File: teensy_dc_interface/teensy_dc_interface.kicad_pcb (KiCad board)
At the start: 2 copper layers, 183 parts, among them J1 3.5mm_Mono_Switched_SymSmall_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, J10 Conn_01x03, J11 Conn_01x03, J12 3.5mm_Mono_Switched_SymSmall_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, J13 3.5mm_Mono_Switched_SymSmall_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, J2 3.5mm_Mono_Switched_SymSmall_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, J3 3.5mm_Mono_Switched_SymSmall_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, J4 3.5mm_Mono_Switched_SymSmall_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, J5 3.5mm_Mono_Switched_SymSmall_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, J6 3.5mm_Mono_Switched_SymSmall_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, J7 3.5mm_Mono_Switched_SymSmall_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, J8 3.5mm_Mono_Switched_SymSmall_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, J9 Conn_01x03, U1 AK4458VN, U2 Teensy4.0, U3 AP65211A, U4 AP62200TWU-7, U5 NE5532, U6 NE5532, U7 NE5532, U8 NE5532, U9 AP65211A

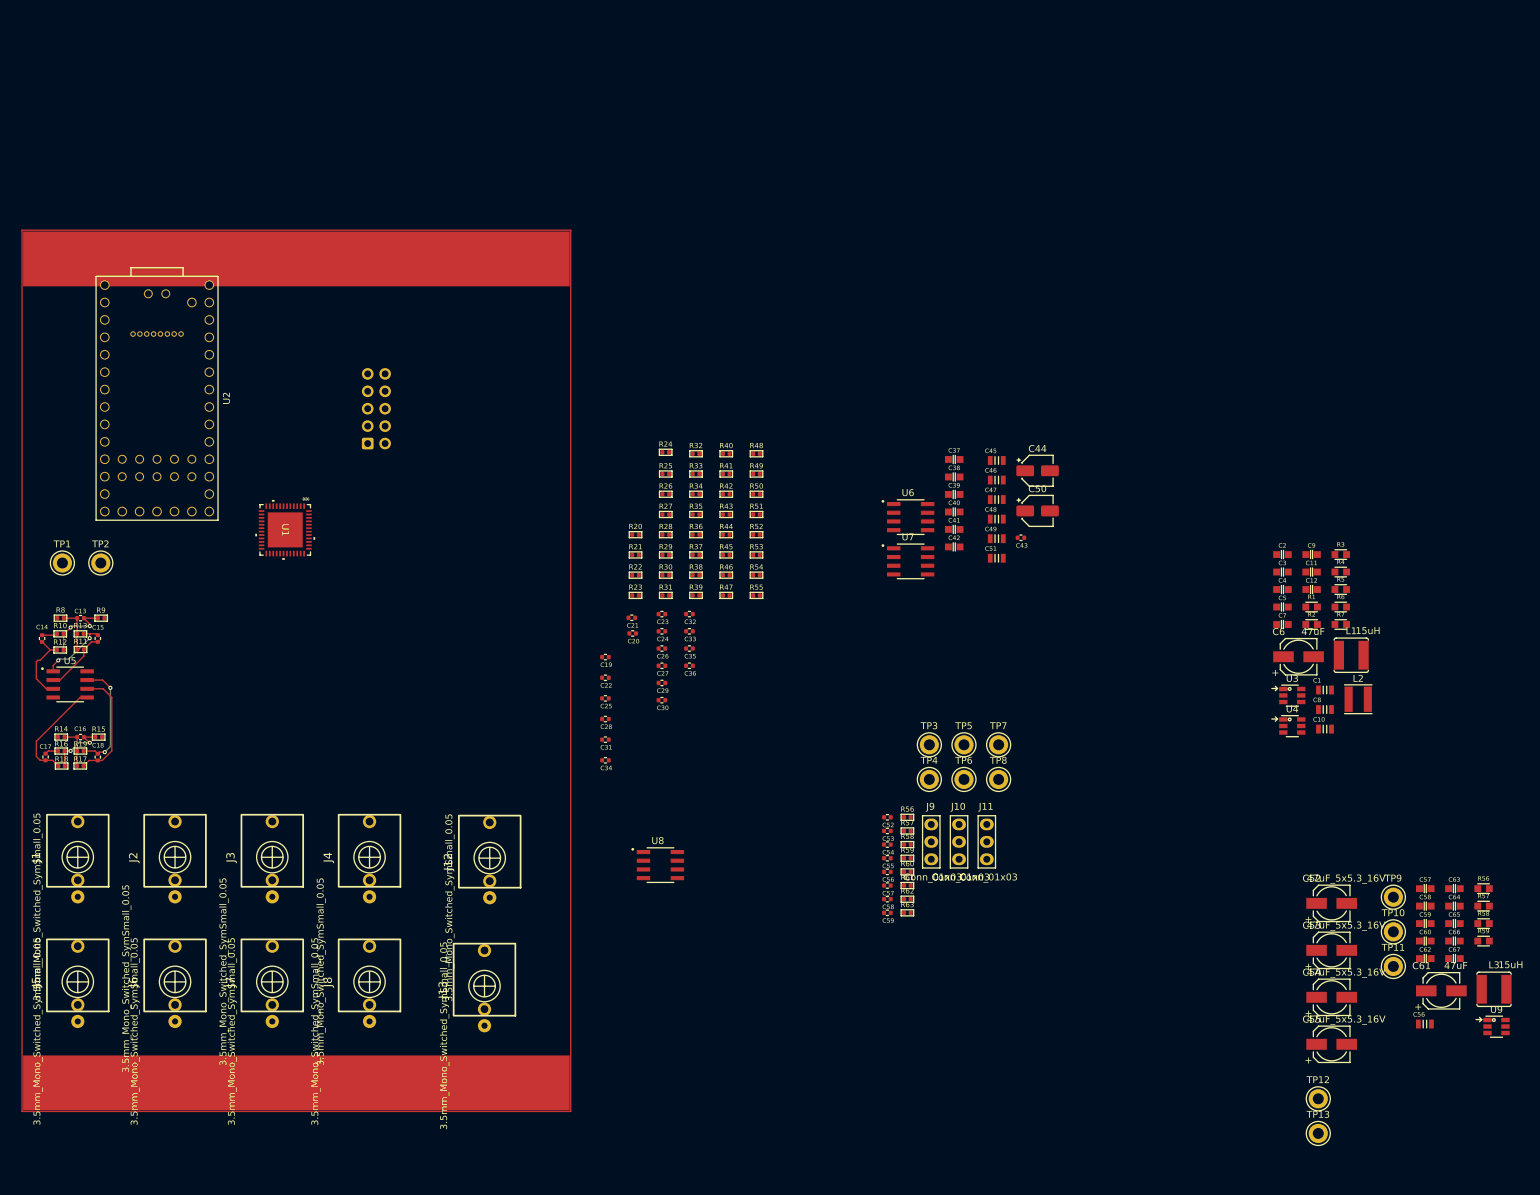
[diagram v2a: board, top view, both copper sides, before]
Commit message: out pairs as pages
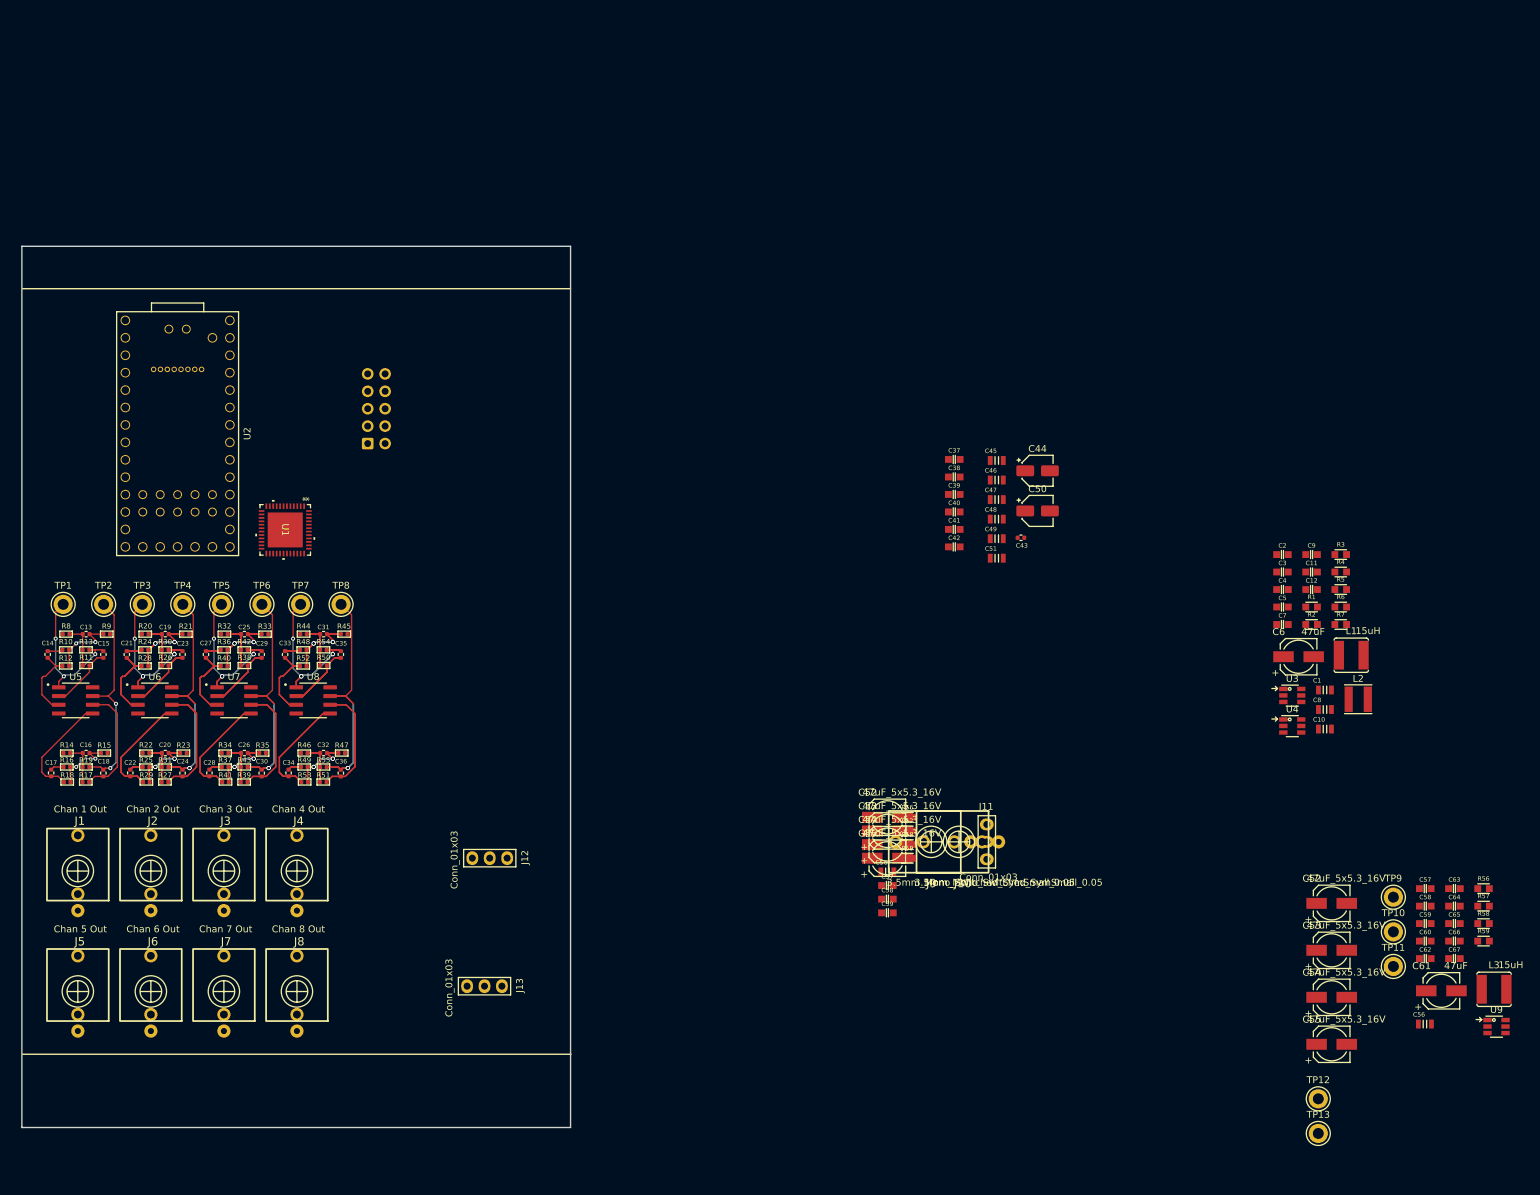
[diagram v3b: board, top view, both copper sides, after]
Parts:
- removed ?: , 
- removed R60, R61, R62, R63: 10R_0402, 4ms_Resistor:R_0402
- removed REF**: Rail_Connection_16HP, 4ms_Faceplate:Rail_Connection_16HP
- C20, C26, C32: value 120p -> 1.0n
- C22, C28, C34: value 1.0n -> 120p
- C52, C53, C54, C55: value 220pF_0402_50V -> 47uF_5x5.3_16V; footprint 4ms_Capacitor:C_0402 -> 4ms_Capacitor:CP_Elec_5x5.3
- C56: value 220pF_0402_50V -> 22uF; footprint 4ms_Capacitor:C_0402 -> 4ms_Capacitor:C_0805
- C57: value 220pF_0402_50V -> 0.1uF; footprint 4ms_Capacitor:C_0402 -> 4ms_Capacitor:C_0603
- C58: value 220pF_0402_50V -> 47pF; footprint 4ms_Capacitor:C_0402 -> 4ms_Capacitor:C_0603
- C59: value 220pF_0402_50V -> 22uF; footprint 4ms_Capacitor:C_0402 -> 4ms_Capacitor:C_0603
- J1: value 3.5mm_Mono_Switched_SymSmall_0.05 -> Chan 1 Out
- J10, J9: value Conn_01x03 -> 3.5mm_Mono_Switched_SymSmall_0.05; footprint 4ms_Connector:Pins_1x03_2.54mm_TH -> 4ms_Jack:EighthInch_PJ398SM
- J12, J13: value 3.5mm_Mono_Switched_SymSmall_0.05 -> Conn_01x03; footprint 4ms_Jack:EighthInch_PJ398SM -> 4ms_Connector:Pins_1x03_2.54mm_TH
- J2: value 3.5mm_Mono_Switched_SymSmall_0.05 -> Chan 2 Out
- J3: value 3.5mm_Mono_Switched_SymSmall_0.05 -> Chan 3 Out
- J4: value 3.5mm_Mono_Switched_SymSmall_0.05 -> Chan 4 Out
- J5: value 3.5mm_Mono_Switched_SymSmall_0.05 -> Chan 5 Out
- J6: value 3.5mm_Mono_Switched_SymSmall_0.05 -> Chan 6 Out
- J7: value 3.5mm_Mono_Switched_SymSmall_0.05 -> Chan 7 Out
- J8: value 3.5mm_Mono_Switched_SymSmall_0.05 -> Chan 8 Out
- R22, R34, R46: value 16.9k -> 3.9k
- R23, R35, R47: value 150 -> 3.9k
- R24, R30, R36, R42, R48, R54: value 150 -> 16.9k
- R26, R27, R38, R39, R50, R51: value 3.9k -> 150
- R28, R40, R52: value 16.9k -> 150
- R56: value 10R_0402 -> 100k; footprint 4ms_Resistor:R_0402 -> 4ms_Resistor:R_0603
- R57: value 10R_0402 -> 75k; footprint 4ms_Resistor:R_0402 -> 4ms_Resistor:R_0603
- R58: value 10R_0402 -> 40.2k; footprint 4ms_Resistor:R_0402 -> 4ms_Resistor:R_0603
- R59: value 10R_0402 -> 7.68k; footprint 4ms_Resistor:R_0402 -> 4ms_Resistor:R_0603
- moved TP3 116.6 mm to (48.7, 73.2)
- moved U6 113.4 mm to (50.5, 87.2)
- moved TP4 111.8 mm to (54.6, 73.2)
- moved TP5 110.2 mm to (60.2, 73.2)
- moved TP6 105.5 mm to (66.1, 73.2)
- moved TP7 103.8 mm to (71.7, 73.2)
- moved U7 100.7 mm to (62.0, 87.2)
- moved TP8 99.2 mm to (77.6, 73.2)
- moved R25 87.0 mm to (49.2, 96.9)
- moved R41 85.7 mm to (60.8, 99.1), turned to 180 degrees
- moved R27 82.8 mm to (52.0, 99.1)
- moved R29 82.7 mm to (49.2, 99.1), turned to 180 degrees
- moved R24 81.2 mm to (49.0, 79.9)
- moved R40 79.5 mm to (60.6, 82.2), turned to 180 degrees
- moved R43 79.3 mm to (63.5, 96.9)
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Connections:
- net AOUTL1N renamed /DAC/AOUTL1N
- net AOUTL2N renamed /DAC/AOUTL2N
- net AOUTR1N renamed /DAC/AOUTR1N
- net OP1_NEG renamed /Outs/Out Pair 1/OP1_NEG
- net OP1_OUT renamed /Outs/Out Pair 1/OP1_OUT
- net OP1_POS renamed /Outs/Out Pair 1/OP1_POS
- net OP2_NEG renamed /Outs/Out Pair 1/OP2_NEG
- net OP2_OUT renamed /Outs/Out Pair 1/OP2_OUT
- net OP2_POS renamed /Outs/Out Pair 1/OP2_POS
- net OP4_OUT renamed /Outs/Out Pair 2/OP2_OUT
- net OP6_OUT renamed /Outs/Out Pair 3/OP2_OUT
- net OP8_OUT renamed /Outs/Out Pair 4/OP2_OUT
- C20 pad 1: OP3_POS -> Net-(C20-Pad1)
- C20 pad 2: AVSS -> Net-(C20-Pad2)
- C21 pad 1: OP3_NEG -> /Outs/Out Pair 2/OP1_POS
- C21 pad 2: OP3_OUT -> AVSS
- C22 pad 1: Net-(C22-Pad1) -> /Outs/Out Pair 2/OP2_POS
- C22 pad 2: Net-(C22-Pad2) -> AVSS
- C23 pad 1: OP4_POS -> /Outs/Out Pair 2/OP1_NEG
- C23 pad 2: AVSS -> /Outs/Out Pair 2/OP1_OUT
- C24 pad 1: OP4_NEG -> /Outs/Out Pair 2/OP2_NEG
- C26 pad 1: OP5_POS -> Net-(C26-Pad1)
- C26 pad 2: AVSS -> Net-(C26-Pad2)
- C27 pad 1: OP5_NEG -> /Outs/Out Pair 3/OP1_POS
- C27 pad 2: OP5_OUT -> AVSS
- C28 pad 1: Net-(C28-Pad1) -> /Outs/Out Pair 3/OP2_POS
- C28 pad 2: Net-(C28-Pad2) -> AVSS
- C29 pad 1: OP6_POS -> /Outs/Out Pair 3/OP1_NEG
- C29 pad 2: AVSS -> /Outs/Out Pair 3/OP1_OUT
- C30 pad 1: OP6_NEG -> /Outs/Out Pair 3/OP2_NEG
- C32 pad 1: OP7_POS -> Net-(C32-Pad1)
- C32 pad 2: AVSS -> Net-(C32-Pad2)
- C33 pad 1: OP7_NEG -> /Outs/Out Pair 4/OP1_POS
- C33 pad 2: OP7_OUT -> AVSS
- C34 pad 1: Net-(C34-Pad1) -> /Outs/Out Pair 4/OP2_POS
- C34 pad 2: Net-(C34-Pad2) -> AVSS
- C35 pad 1: OP8_POS -> /Outs/Out Pair 4/OP1_NEG
- C35 pad 2: AVSS -> /Outs/Out Pair 4/OP1_OUT
- C36 pad 1: OP8_NEG -> /Outs/Out Pair 4/OP2_NEG
- C52 pad 1: AOUTR4P -> AVDD
- C52 pad 2: Net-(C52-Pad2) -> AVSS
- C53 pad 1: AOUTL4P -> AVDD
- C53 pad 2: Net-(C53-Pad2) -> AVSS
- C54 pad 1: AOUTR3P -> AVDD
- C54 pad 2: Net-(C54-Pad2) -> AVSS
- C55 pad 1: AOUTL3P -> AVDD
- C55 pad 2: Net-(C55-Pad2) -> AVSS
- C56 pad 1: AOUTR2P -> +12V
- C56 pad 2: Net-(C56-Pad2) -> AVSS
- C57 pad 1: AOUTL2P -> /Power/SW
- C57 pad 2: Net-(C57-Pad2) -> /Power/BST
- C58 pad 1: AOUTR1P -> /Power/FB
- C58 pad 2: Net-(C58-Pad2) -> TEENSY_5V
- C59 pad 1: AOUTL1P -> TEENSY_5V
- C59 pad 2: Net-(C59-Pad2) -> AVSS
- J10 pad 1: DVSS -> ADC3
- J10 pad 2: SDTI3/DSDR2/TDMO1 -> AVSS
- J10 pad 3: 9_OUT1C -> AVSS
- J11 pad 2: SDTI4/DSDL3/TDMO2 -> SDTI2/DSDL2
- J11 pad 3: 6_OUT1D -> 32_OUT1B
- J12 pad 1: ADC2 -> DVSS
- J12 pad 2: AVSS -> SDTI3/DSDR2/TDMO1
- J12 pad 3: AVSS -> 9_OUT1C
- J13 pad 1: ADC3 -> DVSS
- J13 pad 2: AVSS -> SDTI4/DSDL3/TDMO2
- J13 pad 3: AVSS -> 6_OUT1D
- J3 pad 1: OP3_OUT -> /Outs/Out Pair 2/OP1_OUT
- J5 pad 1: OP5_OUT -> /Outs/Out Pair 3/OP1_OUT
- J7 pad 1: OP7_OUT -> /Outs/Out Pair 4/OP1_OUT
- J9 pad 1: DVSS -> ADC2
- J9 pad 2: SDTI2/DSDL2 -> AVSS
- J9 pad 3: 32_OUT1B -> AVSS
- R15 pad 1: AOUTR1P -> /DAC/AOUTR1P
- R21 pad 1: AOUTL2P -> /DAC/AOUTL2P
- R22 pad 1: AVSS -> /DAC/AOUTR2N
- R22 pad 2: Net-(C19-Pad2) -> Net-(C20-Pad1)
- R23 pad 1: Net-(C19-Pad1) -> /DAC/AOUTR2P
- R23 pad 2: OP3_NEG -> Net-(C20-Pad2)
- R24 pad 1: Net-(C19-Pad2) -> AVSS
- R24 pad 2: OP3_POS -> Net-(C19-Pad2)
- R25 pad 1: Net-(C19-Pad1) -> AVSS
- R25 pad 2: OP3_OUT -> Net-(C20-Pad2)
- R26 pad 1: AOUTR2N -> Net-(C19-Pad1)
- R26 pad 2: Net-(C22-Pad1) -> /Outs/Out Pair 2/OP1_NEG
- R27 pad 1: AOUTR2P -> Net-(C20-Pad1)
- R27 pad 2: Net-(C22-Pad2) -> /Outs/Out Pair 2/OP2_NEG
- R28 pad 1: AVSS -> Net-(C19-Pad2)
- R28 pad 2: Net-(C22-Pad2) -> /Outs/Out Pair 2/OP1_POS
- R29 pad 1: Net-(C22-Pad1) -> Net-(C20-Pad2)
- R29 pad 2: OP4_NEG -> /Outs/Out Pair 2/OP2_POS
- R30 pad 1: Net-(C22-Pad2) -> Net-(C19-Pad1)
- R30 pad 2: OP4_POS -> /Outs/Out Pair 2/OP1_OUT
- R31 pad 1: Net-(C22-Pad1) -> Net-(C20-Pad1)
- R32 pad 1: AOUTL3N -> /DAC/AOUTL3N
- R33 pad 1: AOUTL3P -> /DAC/AOUTL3P
- R34 pad 1: AVSS -> /DAC/AOUTR3N
- R34 pad 2: Net-(C25-Pad2) -> Net-(C26-Pad1)
- R35 pad 1: Net-(C25-Pad1) -> /DAC/AOUTR3P
- R35 pad 2: OP5_NEG -> Net-(C26-Pad2)
- R36 pad 1: Net-(C25-Pad2) -> AVSS
- R36 pad 2: OP5_POS -> Net-(C25-Pad2)
- R37 pad 1: Net-(C25-Pad1) -> AVSS
- R37 pad 2: OP5_OUT -> Net-(C26-Pad2)
- R38 pad 1: AOUTR3N -> Net-(C25-Pad1)
- R38 pad 2: Net-(C28-Pad1) -> /Outs/Out Pair 3/OP1_NEG
- R39 pad 1: AOUTR3P -> Net-(C26-Pad1)
- R39 pad 2: Net-(C28-Pad2) -> /Outs/Out Pair 3/OP2_NEG
- R40 pad 1: AVSS -> Net-(C25-Pad2)
- R40 pad 2: Net-(C28-Pad2) -> /Outs/Out Pair 3/OP1_POS
- R41 pad 1: Net-(C28-Pad1) -> Net-(C26-Pad2)
- R41 pad 2: OP6_NEG -> /Outs/Out Pair 3/OP2_POS
- R42 pad 1: Net-(C28-Pad2) -> Net-(C25-Pad1)
- R42 pad 2: OP6_POS -> /Outs/Out Pair 3/OP1_OUT
- R43 pad 1: Net-(C28-Pad1) -> Net-(C26-Pad1)
- R44 pad 1: AOUTL4N -> /DAC/AOUTL4N
- R45 pad 1: AOUTL4P -> /DAC/AOUTL4P
- R46 pad 1: AVSS -> /DAC/AOUTR4N
- R46 pad 2: Net-(C31-Pad2) -> Net-(C32-Pad1)
- R47 pad 1: Net-(C31-Pad1) -> /DAC/AOUTR4P
- R47 pad 2: OP7_NEG -> Net-(C32-Pad2)
- R48 pad 1: Net-(C31-Pad2) -> AVSS
- R48 pad 2: OP7_POS -> Net-(C31-Pad2)
- R49 pad 1: Net-(C31-Pad1) -> AVSS
- R49 pad 2: OP7_OUT -> Net-(C32-Pad2)
- R50 pad 1: AOUTR4N -> Net-(C31-Pad1)
- R50 pad 2: Net-(C34-Pad1) -> /Outs/Out Pair 4/OP1_NEG
- R51 pad 1: AOUTR4P -> Net-(C32-Pad1)
- R51 pad 2: Net-(C34-Pad2) -> /Outs/Out Pair 4/OP2_NEG
- R52 pad 1: AVSS -> Net-(C31-Pad2)
- R52 pad 2: Net-(C34-Pad2) -> /Outs/Out Pair 4/OP1_POS
- R53 pad 1: Net-(C34-Pad1) -> Net-(C32-Pad2)
- R53 pad 2: OP8_NEG -> /Outs/Out Pair 4/OP2_POS
- R54 pad 1: Net-(C34-Pad2) -> Net-(C31-Pad1)
- R54 pad 2: OP8_POS -> /Outs/Out Pair 4/OP1_OUT
- R55 pad 1: Net-(C34-Pad1) -> Net-(C32-Pad1)
- R56 pad 1: Net-(C52-Pad2) -> /Power/EN
- R56 pad 2: AOUTR4N -> +12V
- R57 pad 1: Net-(C53-Pad2) -> Net-(U9-FB)
- R57 pad 2: AOUTL4N -> /Power/FB
- R58 pad 1: Net-(C54-Pad2) -> /Power/FB
- R58 pad 2: AOUTR3N -> TEENSY_5V
- R59 pad 1: Net-(C55-Pad2) -> AVSS
- R59 pad 2: AOUTL3N -> /Power/FB
- R9 pad 1: AOUTL1P -> /DAC/AOUTL1P
- TP3 pad 1: OP3_OUT -> /Outs/Out Pair 2/OP1_OUT
- TP5 pad 1: OP5_OUT -> /Outs/Out Pair 3/OP1_OUT
- TP7 pad 1: OP7_OUT -> /Outs/Out Pair 4/OP1_OUT
- U1 pad 18: AOUTL1P -> /DAC/AOUTL1P
- U1 pad 23: AOUTR1P -> /DAC/AOUTR1P
- U1 pad 24: AOUTL2P -> /DAC/AOUTL2P
- U1 pad 28: AOUTR2N -> /DAC/AOUTR2N
- U1 pad 29: AOUTR2P -> /DAC/AOUTR2P
- U1 pad 32: AOUTL3P -> /DAC/AOUTL3P
- U1 pad 33: AOUTL3N -> /DAC/AOUTL3N
- U1 pad 36: AOUTR3N -> /DAC/AOUTR3N
- U1 pad 37: AOUTR3P -> /DAC/AOUTR3P
- U1 pad 38: AOUTL4P -> /DAC/AOUTL4P
- U1 pad 39: AOUTL4N -> /DAC/AOUTL4N
- U1 pad 42: AOUTR4N -> /DAC/AOUTR4N
- U1 pad 43: AOUTR4P -> /DAC/AOUTR4P
- U2 pad 33: Teensy_5V -> TEENSY_5V
- U6 pad 1: OP3_OUT -> /Outs/Out Pair 2/OP1_OUT
- U6 pad 2: OP3_NEG -> /Outs/Out Pair 2/OP1_NEG
- U6 pad 3: OP3_POS -> /Outs/Out Pair 2/OP1_POS
- U6 pad 5: OP4_POS -> /Outs/Out Pair 2/OP2_POS
- U6 pad 6: OP4_NEG -> /Outs/Out Pair 2/OP2_NEG
- U7 pad 1: OP5_OUT -> /Outs/Out Pair 3/OP1_OUT
- U7 pad 2: OP5_NEG -> /Outs/Out Pair 3/OP1_NEG
- U7 pad 3: OP5_POS -> /Outs/Out Pair 3/OP1_POS
- U7 pad 5: OP6_POS -> /Outs/Out Pair 3/OP2_POS
- U7 pad 6: OP6_NEG -> /Outs/Out Pair 3/OP2_NEG
- U8 pad 1: OP7_OUT -> /Outs/Out Pair 4/OP1_OUT
- U8 pad 2: OP7_NEG -> /Outs/Out Pair 4/OP1_NEG
- U8 pad 3: OP7_POS -> /Outs/Out Pair 4/OP1_POS
- U8 pad 5: OP8_POS -> /Outs/Out Pair 4/OP2_POS
- U8 pad 6: OP8_NEG -> /Outs/Out Pair 4/OP2_NEG
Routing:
- net /Outs/Out Pair 2/OP2_OUT: track 0.00 -> 48.2 mm, vias 0 -> 2
- net /Outs/Out Pair 3/OP2_OUT: track 0.00 -> 48.2 mm, vias 0 -> 2
- net /Outs/Out Pair 4/OP2_OUT: track 0.00 -> 48.2 mm, vias 0 -> 2
- net /Outs/Out Pair 4/OP2_NEG: track 0.00 -> 33.9 mm
- net /Outs/Out Pair 3/OP2_NEG: track 0.00 -> 33.9 mm
- net /Outs/Out Pair 2/OP2_NEG: track 0.00 -> 33.9 mm
- net /Outs/Out Pair 2/OP1_OUT: track 0.00 -> 32.7 mm, vias 0 -> 5
- net /Outs/Out Pair 3/OP1_OUT: track 0.00 -> 32.7 mm, vias 0 -> 5
- net /Outs/Out Pair 4/OP1_OUT: track 0.00 -> 32.7 mm, vias 0 -> 5
- net /Outs/Out Pair 3/OP2_POS: track 0.00 -> 32.1 mm
- net /Outs/Out Pair 4/OP2_POS: track 0.00 -> 32.1 mm
- net /Outs/Out Pair 2/OP2_POS: track 0.00 -> 32.1 mm
- net AVSS: track 4.20 -> 29.4 mm
- net /Outs/Out Pair 4/OP1_POS: track 0.00 -> 21.8 mm
- net /Outs/Out Pair 2/OP1_POS: track 0.00 -> 21.8 mm
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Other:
- board outline added: 80 x 128.5 mm

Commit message: Added layout for power regulators
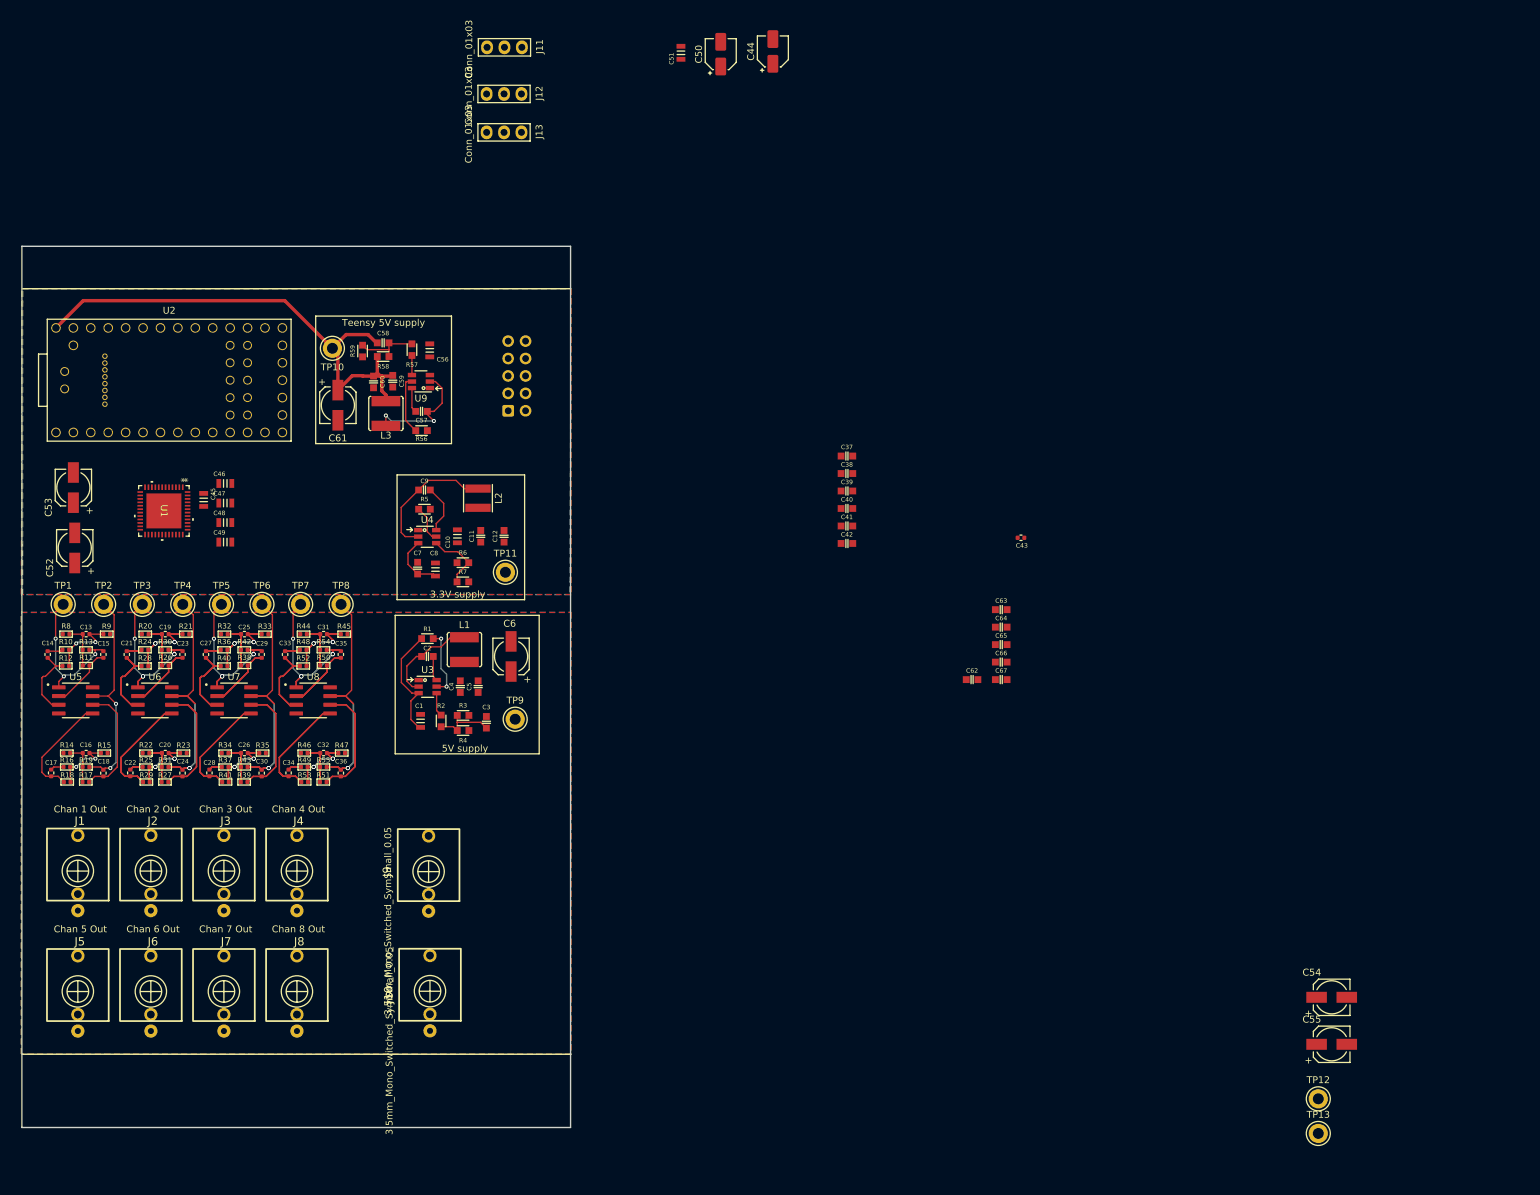
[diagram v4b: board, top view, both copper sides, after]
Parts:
- removed the C52 at (157.3, 104.3)
- removed the C53 at (157.3, 106.3)
- removed the C54 at (157.3, 108.3)
- removed the C55 at (157.3, 110.2)
- removed the C56 at (235.7, 134.4)
- removed the C57 at (157.3, 114.2)
- removed the C58 at (235.7, 117.2)
- removed the C59 at (235.7, 119.8)
- removed the R56 at (244.2, 114.7)
- removed the R57 at (244.2, 117.2)
- removed the R58 at (244.2, 119.8)
- removed the R59 at (244.2, 122.3)
- moved C53 195.5 mm to (38.6, 56.2), turned to 90 degrees
- moved C52 190.5 mm to (38.8, 65.0), turned to 90 degrees
- moved U9 182.9 mm to (89.3, 40.7), turned to 180 degrees
- moved C61 182.2 mm to (77.2, 44.2), turned to -90 degrees
- moved L3 182.1 mm to (84.2, 45.4), turned to 90 degrees
- moved TP10 176.6 mm to (76.4, 35.9), turned to 180 degrees
- moved C60 173.7 mm to (82.4, 40.8), turned to -90 degrees
- moved C57 162.1 mm to (89.4, 45.1), turned to 180 degrees
- moved TP11 141.7 mm to (101.6, 68.5)
- moved J11 135.5 mm to (101.5, -8.00), turned to -90 degrees
- moved R5 134.1 mm to (89.8, 59.4)
- moved C1 132.0 mm to (89.2, 90.2), turned to 90 degrees
- moved L2 131.7 mm to (97.6, 57.8), turned to -90 degrees
- moved C8 131.3 mm to (91.4, 68.2), turned to 90 degrees
- moved TP9 130.7 mm to (103.0, 90.0)
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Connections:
- C56 pad 2: AVSS -> DVSS
- C59 pad 2: AVSS -> DVSS
- C60 pad 2: AVSS -> DVSS
- C61 pad 2: AVSS -> DVSS
- R59 pad 1: AVSS -> DVSS
- U9 pad 1: AVSS -> DVSS
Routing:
- net TEENSY_5V: track 0.00 -> 75.0 mm
- net /Power/SW: track 0.00 -> 51.7 mm, vias 0 -> 2
- net /Power/FB: track 0.00 -> 28.3 mm
- net +12V: track 0.00 -> 25.4 mm
- net /Power/EN: track 0.00 -> 18.5 mm, vias 0 -> 2
- net /Power/BST: track 0.00 -> 7.28 mm
- net Net-(U4-BST): track 0.00 -> 7.11 mm
- net Net-(U4-EN): track 0.00 -> 5.40 mm
- net Net-(U3-FB): track 0.00 -> 3.47 mm
- net Net-(U9-FB): track 0.00 -> 2.85 mm
- added copper zone on B.Cu, net AVSS
- added copper zone on F.Cu, net AVSS
- added copper zone on B.Cu, net DVSS
- added copper zone on F.Cu, net DVSS
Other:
- board text added: "3.3V supply"
- board text added: "5V supply"
- board text added: "Teensy 5V supply"
